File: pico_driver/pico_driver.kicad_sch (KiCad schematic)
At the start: 22 parts, among them J1 GPIO, J2 Conn_SERVO, J3 Conn_ESC, J4 Conn_01x12_Pin, J5 PICO_5VOUT, SW1 SW_SPDT, SW4 SW_Push, SW5 SW_Push, U1 CAT24C256, U2 Pico

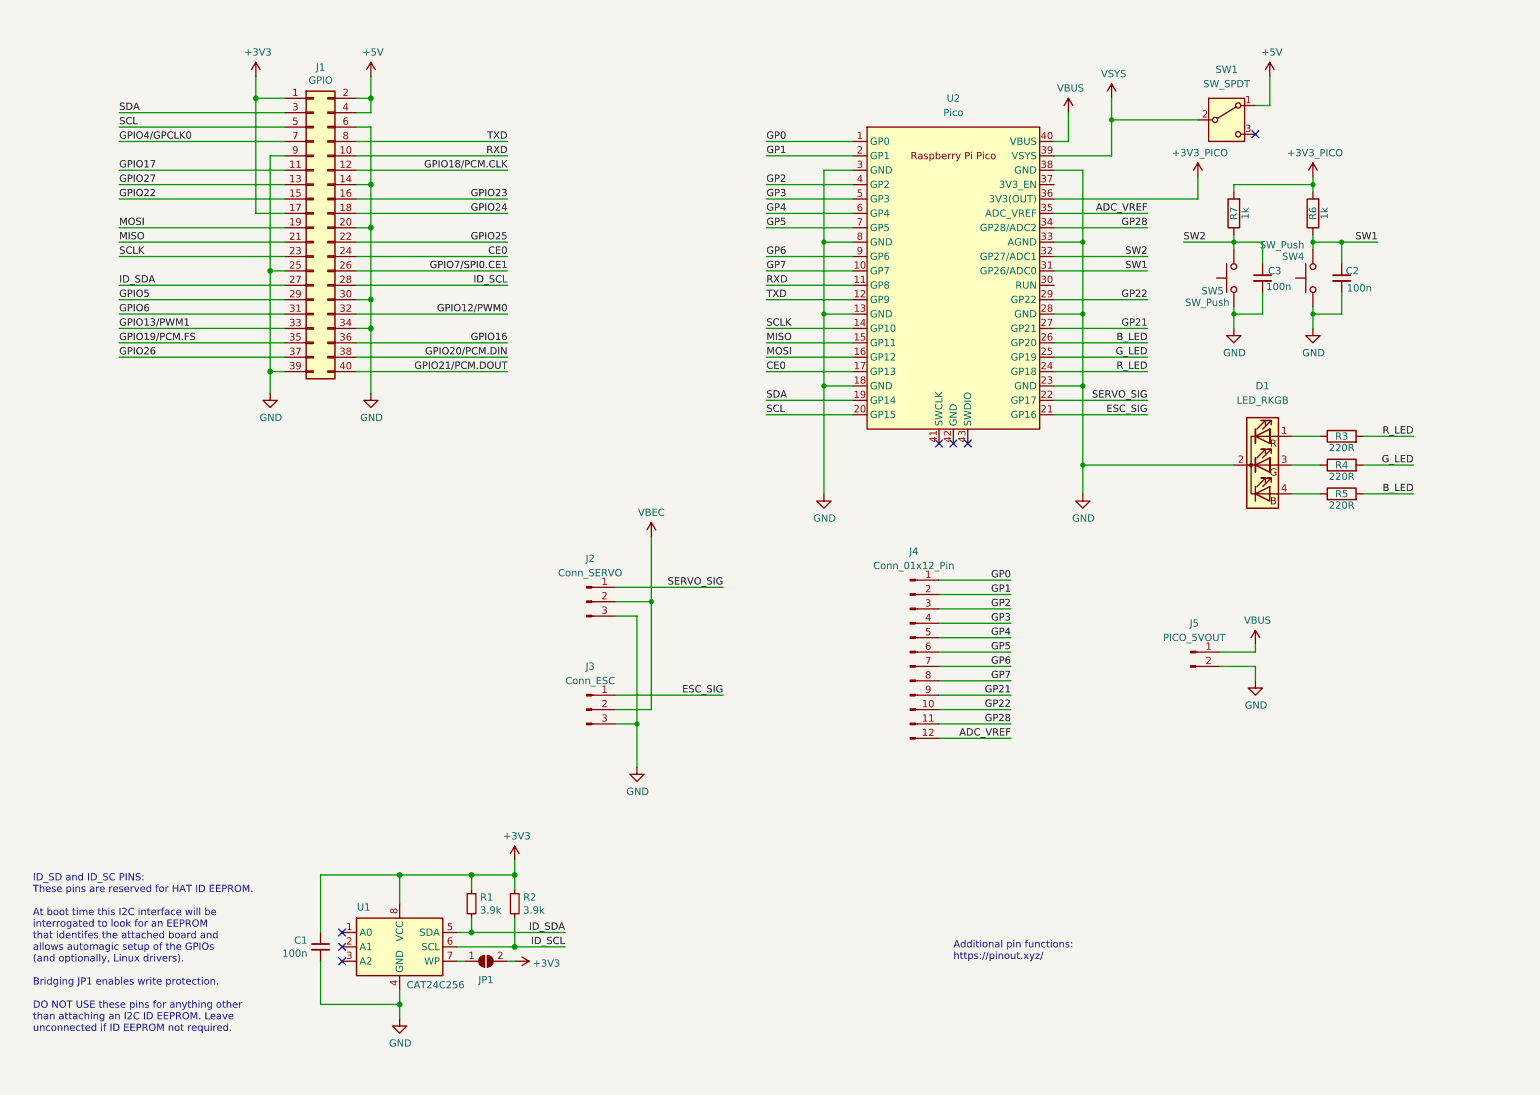
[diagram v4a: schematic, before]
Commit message: update schematic
removed eeprom
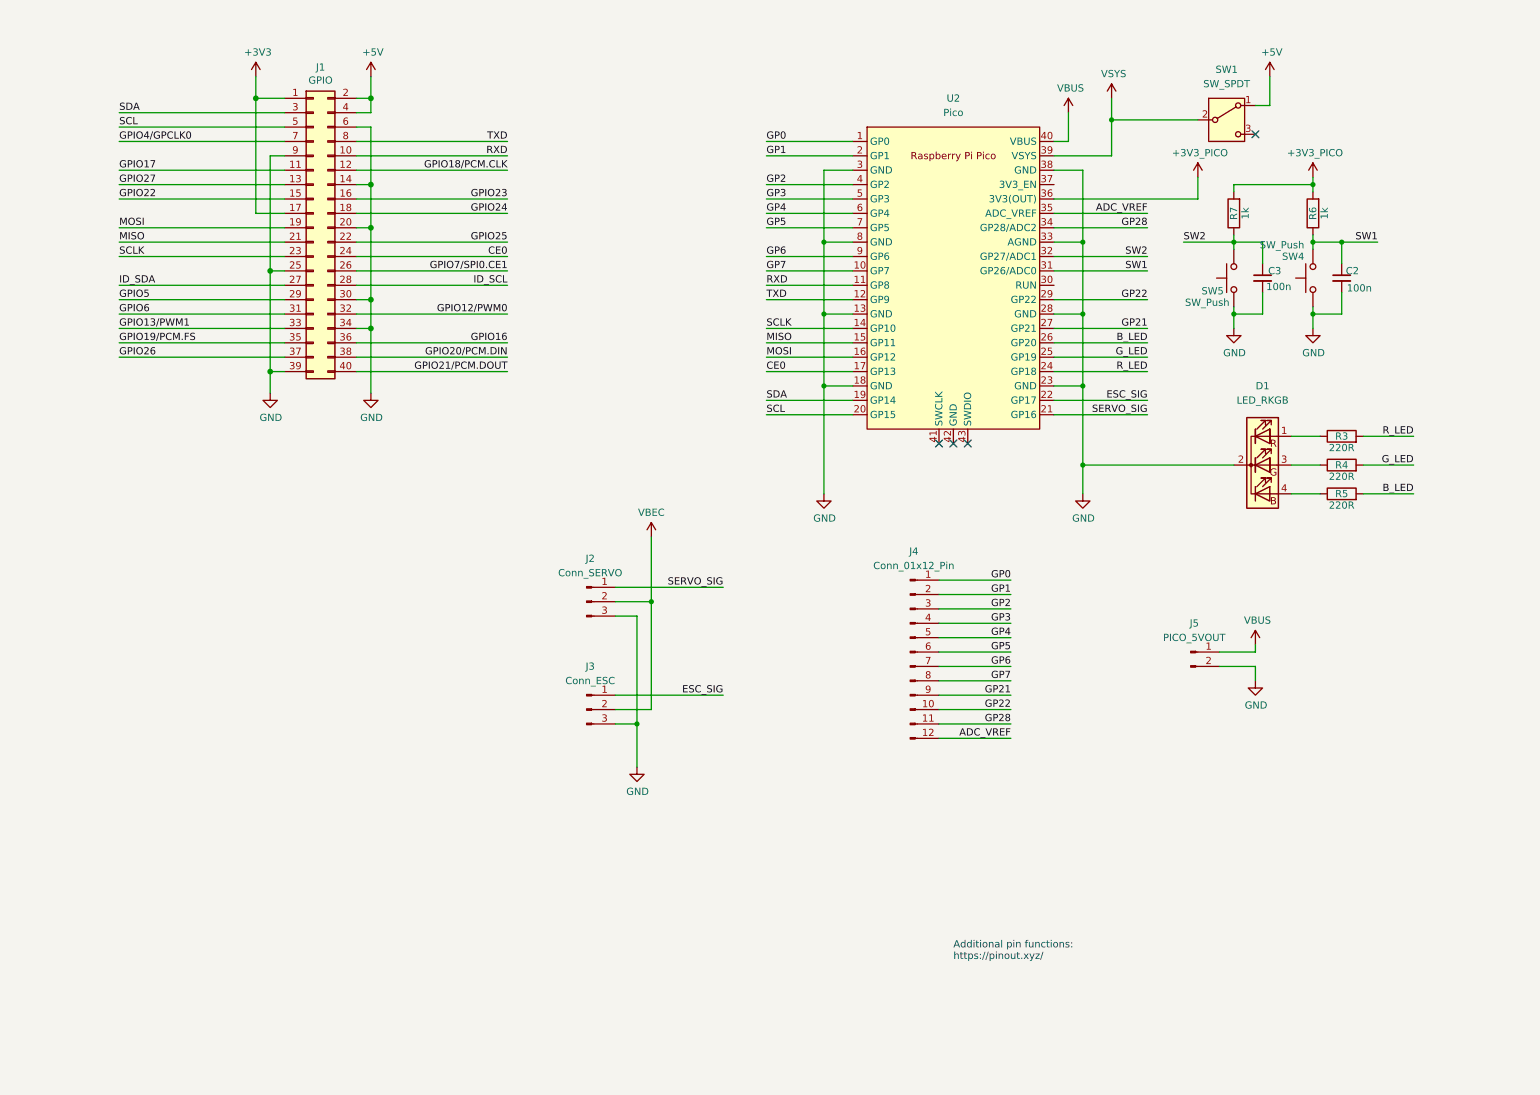
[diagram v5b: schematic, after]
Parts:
- removed C1: 100n, Capacitor_SMD:C_0805_2012Metric, symbol Device:C_Small
- removed JP1: ID_WP, Jumper:SolderJumper-2_P1.3mm_Bridged_Pad1.0x1.5mm, symbol Jumper:SolderJumper_2_Open
- removed R1, R2: 3.9k, Resistor_SMD:R_1206_3216Metric, symbol Device:R_Small
- removed U1: CAT24C256, CAT24C256:TSSOP8_4P50X3P10_ONS, symbol Memory_EEPROM:CAT24C256
- C2, C3: footprint Capacitor_SMD:C_0805_2012Metric -> Capacitor_SMD:C_0805_2012Metric_Pad1.18x1.45mm_HandSolder
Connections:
- net ESC_SIG: now also U2.22 (GP17); no longer U2.21 (GP16)
- net SERVO_SIG: now also U2.21 (GP16); no longer U2.22 (GP17)
- no-connect marks 7 -> 4
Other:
- note removed: "ID_SD and ID_SC PINS: These pins are reserved for HAT ID EEPROM. At boot time this I2C interface will be interrogated to look for an EEPROM that identifes the attached board and allows automagic setup of the GPIOs (and optionally, Linux drivers). Bridging JP1 enables write protection. DO NOT USE these pins for anything other than attaching an I2C ID EEPROM. Leave unconnected if ID EEPROM not requ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"

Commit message: update pico footprint
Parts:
- U2: footprint Pico:RPi_Pico_SMD_TH -> RaspberryPi_Pico:RaspberryPi_Pico_Common_THT
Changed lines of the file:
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@@
 			)
 		)
-		(property "Footprint" "Pico:RPi_Pico_SMD_TH"
+		(property "Footprint" "RaspberryPi_Pico:RaspberryPi_Pico_Common_THT"
 			(at 179.07 59.69 90)
 			(effects

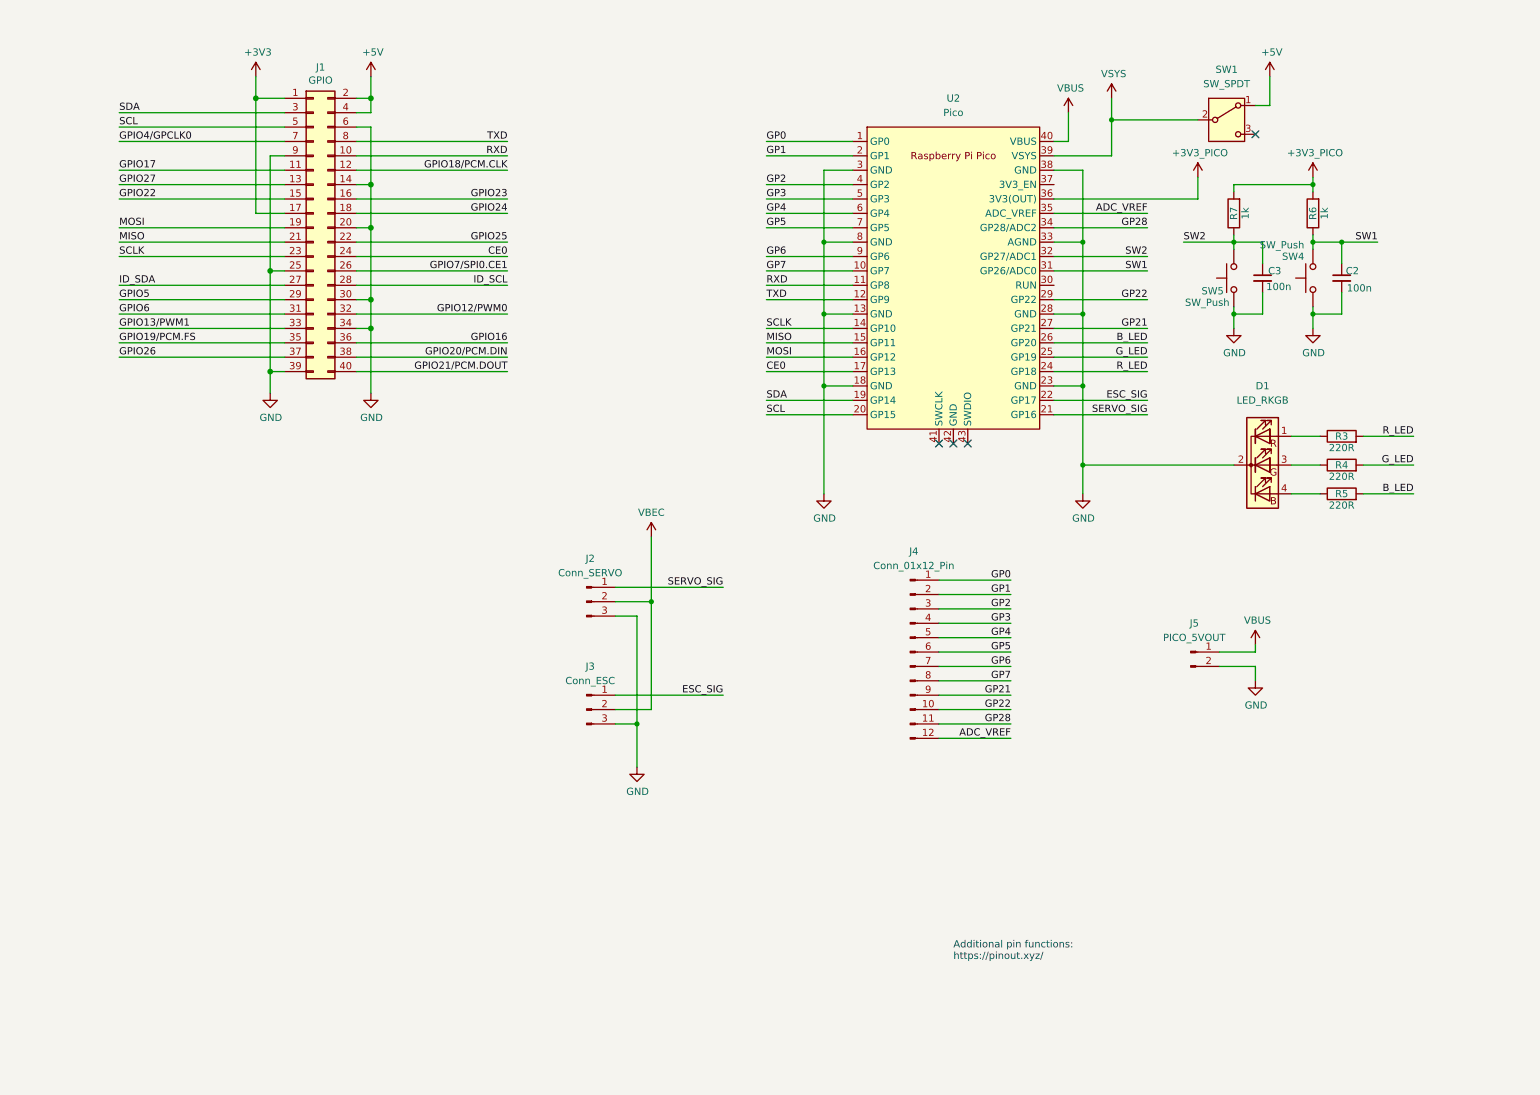
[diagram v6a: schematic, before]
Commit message: update schematic
- updated wiring
- added more breakout connector pins
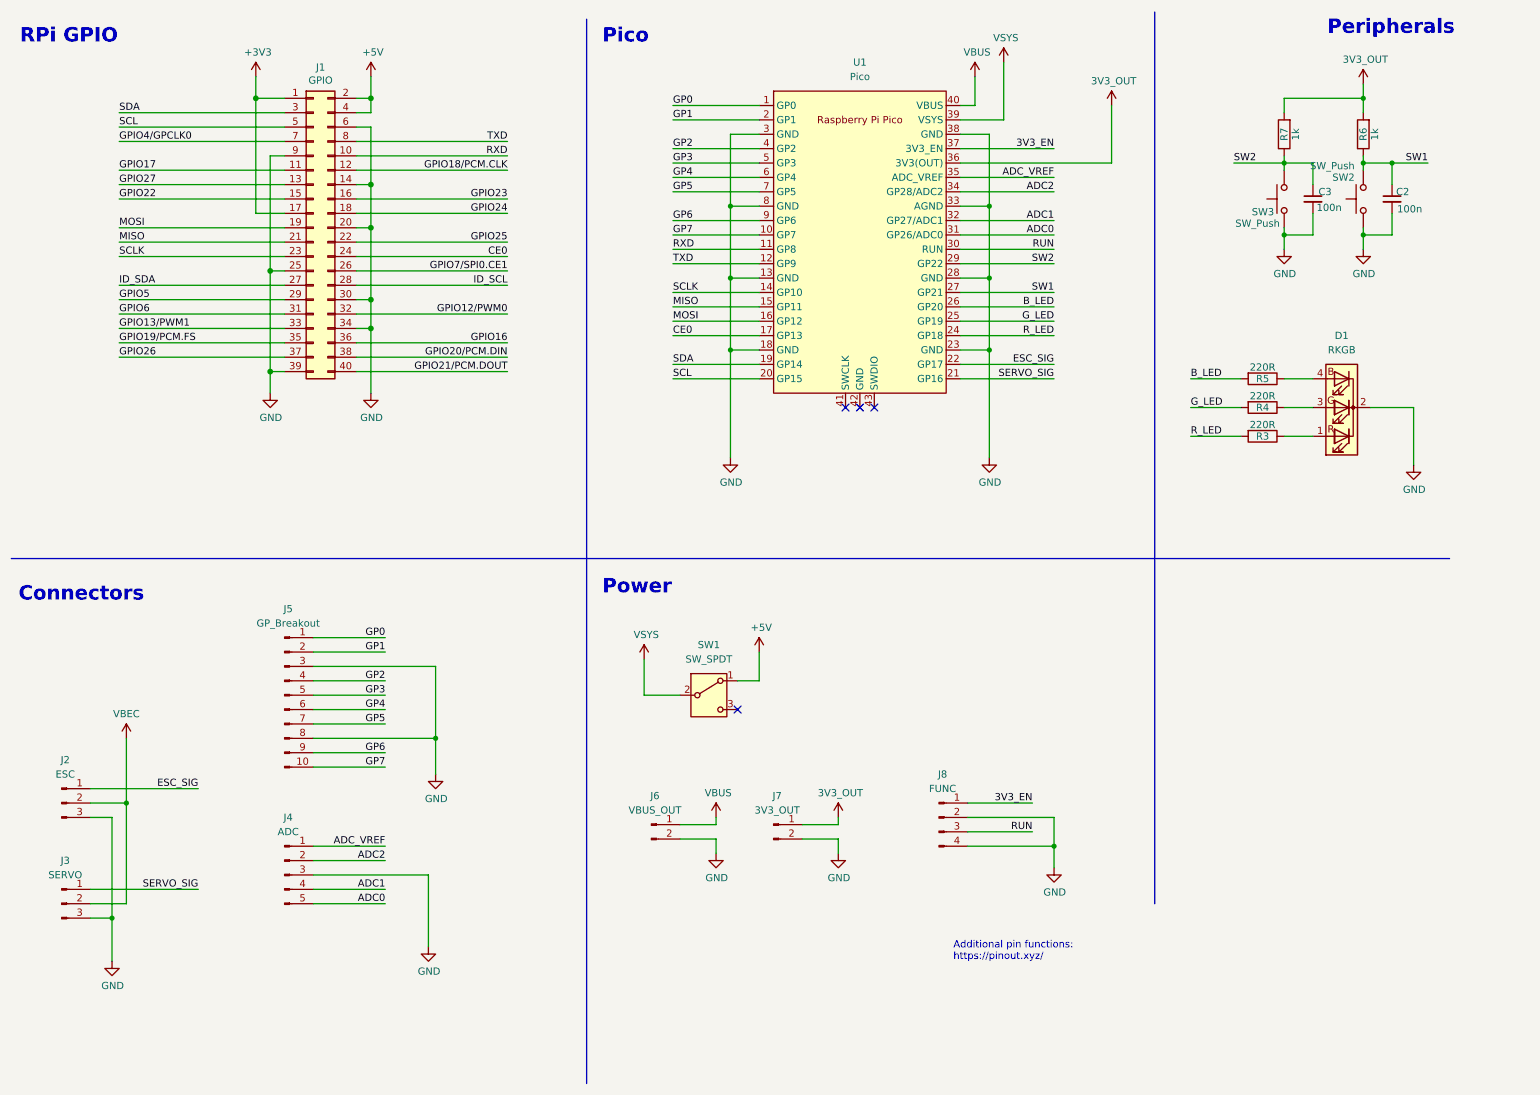
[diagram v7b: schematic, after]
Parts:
- removed J4: Conn_01x12_Pin, Connector_PinHeader_2.54mm:PinHeader_1x12_P2.54mm_Vertical, symbol Connector:Conn_01x12_Pin
- added J4: ADC, Connector_PinHeader_2.54mm:PinHeader_1x05_P2.54mm_Vertical, symbol Connector:Conn_01x05_Pin
- added J5: GP_Breakout, Connector_PinHeader_2.54mm:PinHeader_1x10_P2.54mm_Vertical, symbol Connector:Conn_01x10_Pin
- added J7: 3V3_OUT, Connector_PinHeader_2.54mm:PinHeader_1x02_P2.54mm_Vertical, symbol Connector:Conn_01x02_Pin
- added J8: FUNC, Connector_PinHeader_2.54mm:PinHeader_1x04_P2.54mm_Vertical, symbol Connector:Conn_01x04_Pin
- D1: value LED_RKGB -> RKGB
- J2: value Conn_SERVO -> ESC
- J3: value Conn_ESC -> SERVO
- J6: renamed from J5; value PICO_5VOUT -> VBUS_OUT
- renumbered SW4 to SW2, SW5 to SW3, U2 to U1
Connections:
- net GP21 is gone; now on net SW1: U1.27 (GP21)
- net GP22 is gone; now on net SW2: U1.29 (GP22)
- net ADC_VREF: now also J4.1 (Pin_1)
- net ESC_SIG: now also J2.1 (Pin_1); no longer J3.1 (Pin_1)
- net GND: now also J4.3 (Pin_3), J5.3 (Pin_3), J5.8 (Pin_8), J7.2 (Pin_2), J8.2 (Pin_2), J8.4 (Pin_4)
- net GP0: now also J5.1 (Pin_1)
- net GP1: now also J5.2 (Pin_2)
- net GP2: now also J5.4 (Pin_4)
- net GP3: now also J5.5 (Pin_5)
- net GP4: now also J5.6 (Pin_6)
- net GP5: now also J5.7 (Pin_7)
- net GP6: now also J5.9 (Pin_9)
- net GP7: now also J5.10 (Pin_10)
- net SERVO_SIG: now also J3.1 (Pin_1); no longer J2.1 (Pin_1)
- net SW1: no longer U1.31 (GP26/ADC0)
- net SW2: no longer U1.32 (GP27/ADC1)
- net RUN: now reaches U1.30 (RUN)
- net RUN: now also J8.3 (Pin_3)
- net 3V3_EN: now reaches U1.37 (3V3_EN)
- net 3V3_EN: now also J8.1 (Pin_1)
- net +3V3_PICO renamed 3V3_OUT
- net 3V3_OUT: now also J7.1 (Pin_1)
- net GP28 renamed ADC2
- net ADC2: now also J4.2 (Pin_2)
- new net ADC0: J4.5 (Pin_5), U1.31 (GP26/ADC0)
- new net ADC1: J4.4 (Pin_4), U1.32 (GP27/ADC1)
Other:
- note added: "Connectors"
- note added: "Peripherals"
- note added: "Pico"
- note added: "Power"
- note added: "RPi GPIO"
- moved on the sheet: C2, C3, D1, J2, J3, J6, R3, R4, R5, R6, R7, SW1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

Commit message: update pcb layout
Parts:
- J2: value ESC -> SRV; footprint Connector_PinHeader_2.54mm:PinHeader_1x03_P2.54mm_Vertical -> Connector_PinHeader_2.54mm:PinHeader_1x03_P2.54mm_Horizontal
- J3: value SERVO -> ESC
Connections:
- net +5V: now also SW1.3 (C); no longer SW1.1 (A)
- net ESC_SIG: now also J3.3 (Pin_3), U1.21 (GP16); no longer J2.1 (Pin_1), U1.22 (GP17)
- net GND: now also J2.1 (Pin_1), J3.1 (Pin_1); no longer J2.3 (Pin_3), J3.3 (Pin_3)
- net SERVO_SIG: now also J2.3 (Pin_3), U1.22 (GP17); no longer J3.1 (Pin_1), U1.21 (GP16)
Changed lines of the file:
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@@
 	)
 	(junction
-		(at 139.7 72.39)
+		(at 30.48 167.64)
 		(diameter 0)
 		(color 0 0 0 0)
 	)
 	(junction
-		(at 30.48 172.72)
+		(at 139.7 72.39)
 		(diameter 0)
 		(color 0 0 0 0)
@@
 	)
 	(no_connect
-		(at 162.56 82.55)
+		(at 140.97 130.81)
 	)
 	(no_connect
-		(at 140.97 135.89)
+		(at 162.56 82.55)
 	)
 	(no_connect
@@
 	(wire
 		(pts
+			(xy 26.67 167.64) (xy 30.48 167.64)
+		)
+		(stroke
+			(width 0)
+			(type default)
+		)
+	)
+	(wire
+		(pts
 			(xy 58.42 38.1) (xy 60.96 38.1)
 		)
@@
 	(wire
 		(pts
-			(xy 30.48 154.94) (xy 30.48 172.72)
-		)
-		(stroke
-			(width 0)
-			(type default)
-		)
-	)
-	(wire
-		(pts
 			(xy 31.75 63.5) (xy 60.96 63.5)
 		)
@@
 	(wire
 		(pts
-			(xy 144.78 130.81) (xy 140.97 130.81)
-		)
-		(stroke
-			(width 0)
-			(type default)
-		)
-	)
-	(wire
-		(pts
 			(xy 87.63 128.27) (xy 87.63 140.97)
 		)
@@
 	(wire
 		(pts
+			(xy 30.48 149.86) (xy 30.48 167.64)
+		)
+		(stroke
+			(width 0)
+			(type default)
+		)
+	)
+	(wire
+		(pts
 			(xy 124.46 127) (xy 124.46 133.35)
 		)
@@
 	(wire
 		(pts
-			(xy 144.78 125.73) (xy 144.78 130.81)
+			(xy 144.78 125.73) (xy 144.78 135.89)
 		)
 		(stroke
@@
 	(wire
 		(pts
-			(xy 180.34 69.85) (xy 196.85 69.85)
+			(xy 26.67 149.86) (xy 30.48 149.86)
 		)
 		(stroke
@@
 	(wire
 		(pts
-			(xy 129.54 54.61) (xy 144.78 54.61)
+			(xy 180.34 69.85) (xy 196.85 69.85)
 		)
 		(stroke
@@
 	(wire
 		(pts
-			(xy 31.75 71.12) (xy 60.96 71.12)
+			(xy 129.54 54.61) (xy 144.78 54.61)
 		)
 		(stroke
 			(width 0)
-			(type solid)
+			(type default)
 		)
 	)
 	(wire
 		(pts
-			(xy 182.88 29.21) (xy 182.88 24.13)
+			(xy 31.75 71.12) (xy 60.96 71.12)
 		)
 		(stroke
 			(width 0)
-			(type default)
+			(type solid)
 		)
 	)
 	(wire
 		(pts
-			(xy 30.48 172.72) (xy 30.48 180.34)
+			(xy 182.88 29.21) (xy 182.88 24.13)
 		)
 		(stroke
@@
 	(wire
 		(pts
-			(xy 26.67 149.86) (xy 45.72 149.86)
+			(xy 30.48 167.64) (xy 30.48 180.34)
 		)
 		(stroke
@@
 	(wire
 		(pts
-			(xy 26.67 172.72) (xy 30.48 172.72)
-		)
-		(stroke
-			(width 0)
-			(type default)
-		)
-	)
-	(wire
-		(pts
 			(xy 129.54 29.21) (xy 144.78 29.21)
 		)
@@
 	(wire
 		(pts
-			(xy 26.67 154.94) (xy 30.48 154.94)
+			(xy 26.67 154.94) (xy 44.45 154.94)
 		)
 		(stroke
@@
 	(wire
 		(pts
+			(xy 26.67 172.72) (xy 45.72 172.72)
+		)
+		(stroke
+			(width 0)
+			(type default)
+		)
+	)
+	(wire
+		(pts
 			(xy 152.4 158.75) (xy 158.75 158.75)
 		)
@@
 	(wire
 		(pts
-			(xy 26.67 167.64) (xy 45.72 167.64)
+			(xy 144.78 135.89) (xy 140.97 135.89)
 		)
 		(stroke
@@
 		)
 	)
+	(label "ESC_SIG"
+		(at 196.85 77.47 180)
+		(effects
+			(font
+				(size 1.27 1.27)
+			)
+			(justify right bottom)
+		)
+	)
 	(label "ADC1"
 		(at 78.74 167.64 180)
@@
 		)
 	)
-	(label "SW2"
-		(at 196.85 57.15 180)
+	(label "SERVO_SIG"
+		(at 44.45 154.94 180)
 		(effects
 			(font
@@
 		)
 	)
-	(label "GPIO23"
-		(at 100.33 45.72 180)
+	(label "SW2"
+		(at 196.85 57.15 180)
 		(effects
 			(font
@@
 		)
 	)
-	(label "SERVO_SIG"
-		(at 196.85 77.47 180)
+	(label "GPIO23"
+		(at 100.33 45.72 180)
 		(effects
 			(font
@@
 		)
 	)
-	(label "ESC_SIG"
-		(at 45.72 149.86 180)
-		(effects
-			(font
-				(size 1.27 1.27)
-			)
-			(justify right bottom)
-		)
-	)
 	(label "GPIO22"
 		(at 31.75 45.72 0)
@@
 		)
 	)
-	(label "ESC_SIG"
-		(at 196.85 74.93 180)
-		(effects
-			(font
-				(size 1.27 1.27)
-			)
-			(justify right bottom)
-		)
-	)
 	(label "GPIO17"
 		(at 31.75 40.64 0)
@@
 		)
 	)
+	(label "SERVO_SIG"
+		(at 196.85 74.93 180)
+		(effects
+			(font
+				(size 1.27 1.27)
+			)
+			(justify right bottom)
+		)
+	)
 	(label "RUN"
 		(at 196.85 54.61 180)
@@
 		)
 	)
-	(label "SERVO_SIG"
-		(at 45.72 167.64 180)
-		(effects
-			(font
-				(size 1.27 1.27)
-			)
-			(justify right bottom)
-		)
-	)
 	(label "SCLK"
 		(at 31.75 55.88 0)
@@
 		)
 	)
+	(label "ESC_SIG"
+		(at 45.72 172.72 180)
+		(effects
+			(font
+				(size 1.27 1.27)
+			)
+			(justify right bottom)
+		)
+	)
 	(label "GP1"
 		(at 78.74 125.73 180)
@@
 			)
 		)
-		(property "Value" "SERVO"
+		(property "Value" "ESC"
 			(at 22.225 165.1 0)
 			(effects
@@
 			)
 		)
-		(property "Value" "ESC"
+		(property "Value" "SRV"
 			(at 22.225 147.32 0)
 			(effects
@@
 			)
 		)
-		(property "Footprint" "Connector_PinHeader_2.54mm:PinHeader_1x03_P2.54mm_Vertical"
+		(property "Footprint" "Connector_PinHeader_2.54mm:PinHeader_1x03_P2.54mm_Horizontal"
 			(at 21.59 152.4 0)
 			(effects
